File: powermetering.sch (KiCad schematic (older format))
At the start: 143 parts, among them J1 Conn_01x04, J2 Conn_01x02, J3 Conn_01x02, J4 Conn_01x02, J5 Conn_01x02, T1 Transformer_1P_1S, T2 Transformer_1P_1S, T3 Transformer_1P_1S, U2 ADE9000, U7 LTC4055, Y1 Crystal

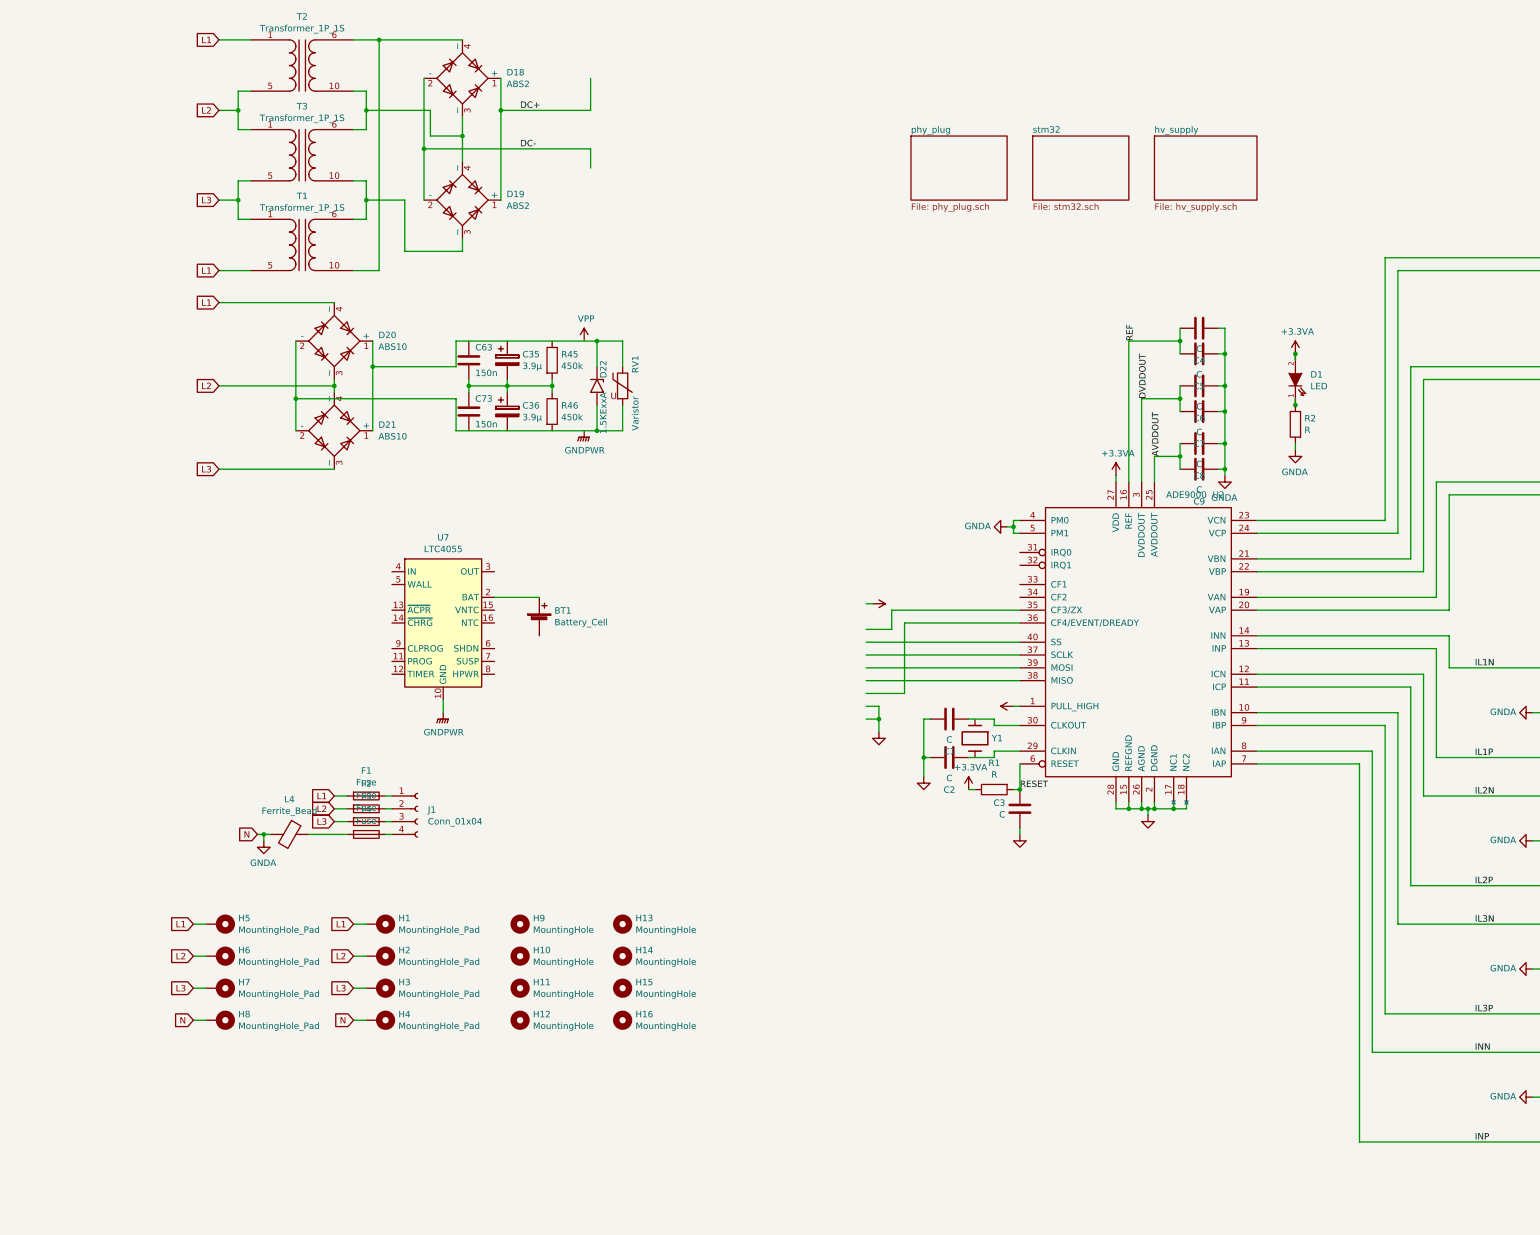
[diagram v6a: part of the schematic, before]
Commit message: add supply and AFE isolation
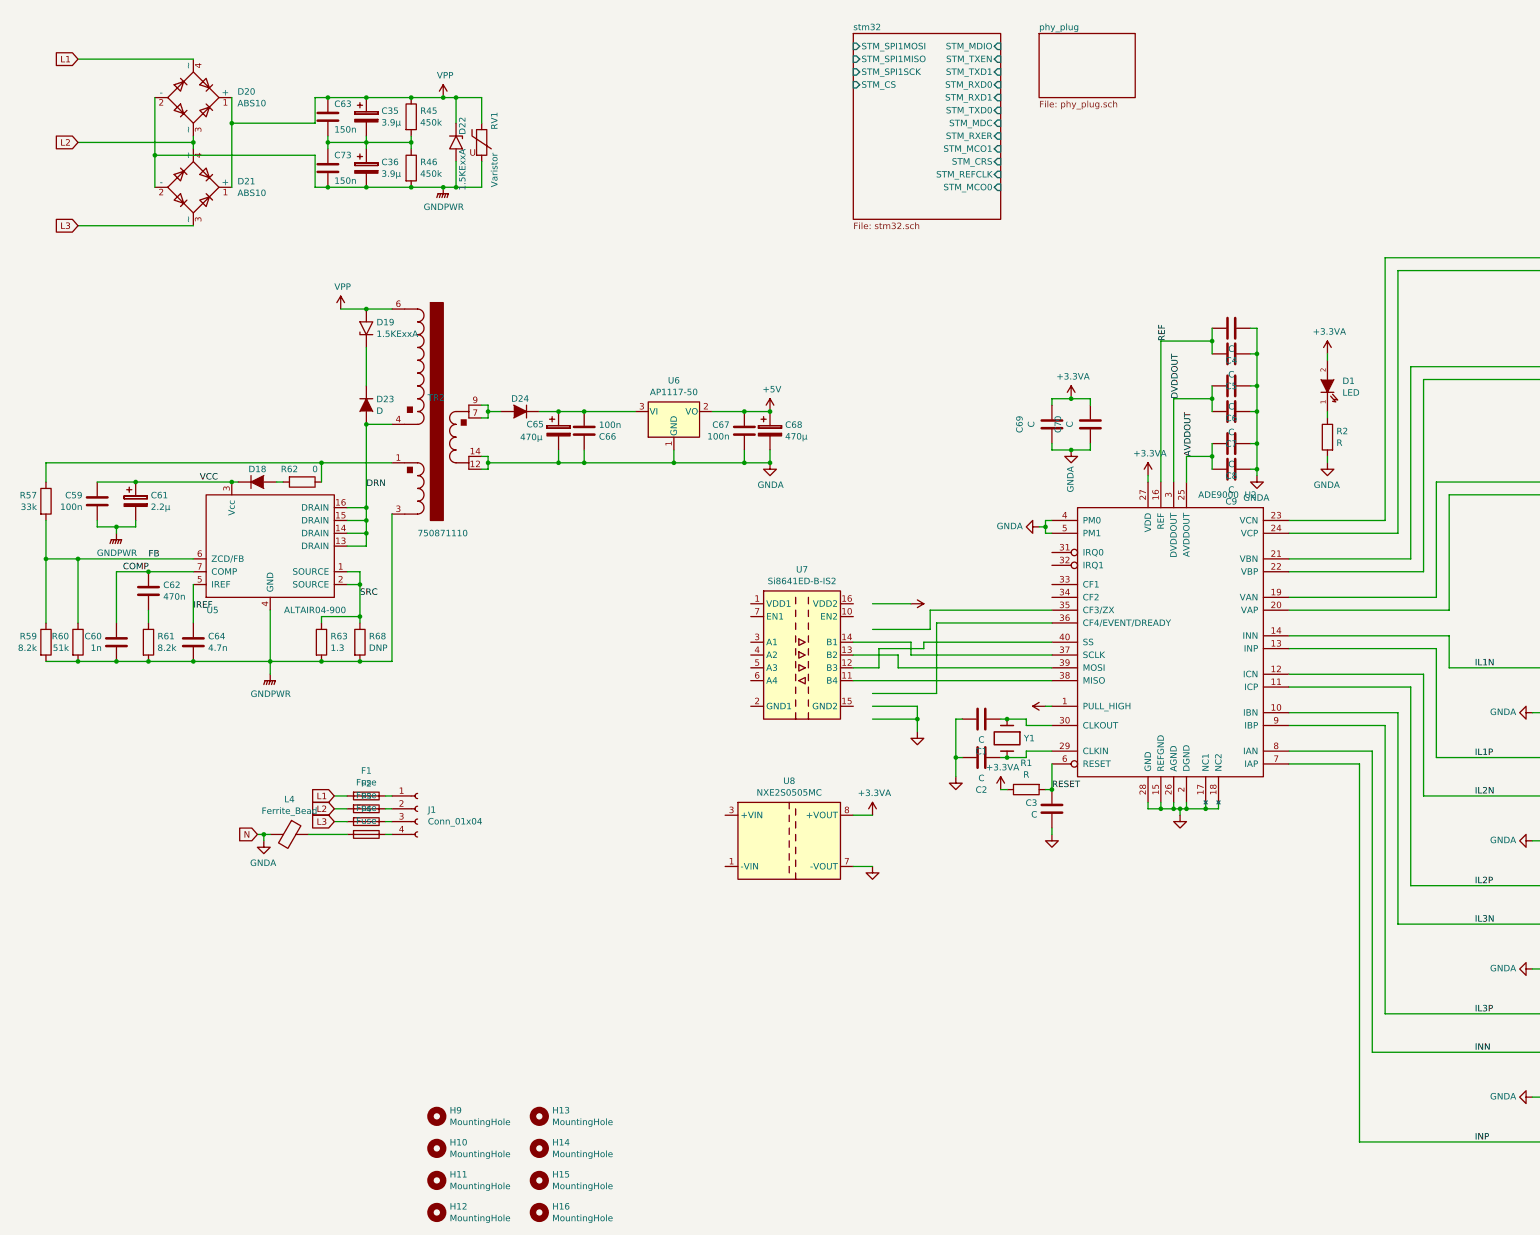
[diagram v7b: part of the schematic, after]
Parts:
- removed BT1: Battery_Cell, Battery:BatteryHolder_Keystone_1042_1x18650, symbol Device:Battery_Cell
- removed D18, D19: ABS2, Diode_SMD:Diode_Bridge_Diotec_ABS, symbol Diode_Bridge:ABS2
- removed H1, H2, H3, H4, H5, H6, H7, H8: MountingHole_Pad, MountingHole:MountingHole_3.2mm_M3_DIN965_Pad, symbol Mechanical:MountingHole_Pad
- removed T1, T2, T3: Transformer_1P_1S, Transformer_THT:Transformer_CHK_EI30-2VA_1xSec, symbol powermetering:Transformer_1P_1S
- removed U7: LTC4055, Package_DFN_QFN:QFN-16-1EP_4x4mm_P0.65mm_EP2.15x2.15mm, symbol Battery_Management:LTC4055
- added C59, C66, C67: 100n, stmbl:C_0805, symbol stmbl:C
- added C60: 1n, stmbl:C_0805, symbol stmbl:C
- added C61: 2.2µ, stmbl:C_1206, symbol stmbl:CP
- added C62: 470n, stmbl:C_0805, symbol stmbl:C
- added C64: 4.7n, stmbl:C_0805, symbol stmbl:C
- added C65: 470µ, Capacitor_SMD:CP_Elec_8x10, symbol stmbl:CP
- added C68: 470µ, Capacitor_SMD:CP_Elec_8x10.5, symbol stmbl:CP
- added C69, C70: C, stmbl:C_0603, symbol stmbl:C
- added D18, D23, D24: D, stmbl:SMA_Standard, symbol stmbl:D
- added D19: 1.5KExxA, stmbl:SMA_Standard, symbol Diode:1.5KExxA
- added R57: 33k, stmbl:R_0805, symbol stmbl:R
- added R59, R61: 8.2k, stmbl:R_0805, symbol stmbl:R
- added R60: 51k, stmbl:R_0805, symbol stmbl:R
- added R62: 0, stmbl:R_0805, symbol stmbl:R
- added R63: 1.3, stmbl:R_1206, symbol stmbl:R
- added R68: DNP, stmbl:R_1206, symbol stmbl:R
- added TR2: 750871110, altair04:750871110, symbol altair04:TRANSFO
- added U5: ALTAIR04-900, Package_SO:SOIC-16_3.9x9.9mm_P1.27mm, symbol altair04:ALTAIR04-900
- added U6: AP1117-50, Package_TO_SOT_SMD:SOT-223-3_TabPin2, symbol Regulator_Linear:AP1117-50
- added U7: Si8641ED-B-IS2, Package_SO:SOIC-16W_7.5x10.3mm_P1.27mm, symbol Isolator:Si8641ED-B-IS2
- added U8: NXE2S0505MC, Converter_DCDC:Converter_DCDC_muRata_NXE2SxxxxMC_THT, symbol Regulator_Switching:NXE2S0505MC
- C1, C10, C11, C12, C13, C14, C15, C16, C17, C18, C19, C2, C20, C21, C22, C23, C24, C25, C26, C27, C28, C29, C3, C30, C31, C32, C33, C34, C4, C5, C6, C7, C8, C9: footprint stmbl-kicad-lib:C_0603 -> stmbl:C_0603
- D10, D11, D12, D13, D14, D15, D16, D17, D2, D3, D4, D5, D6, D7, D8, D9: footprint stmbl-kicad-lib:SMA_Standard -> stmbl:SMA_Standard
- D22: footprint Diode_THT:D_DO-201AE_P15.24mm_Horizontal -> stmbl:SMA_Standard
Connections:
- net labels added: +5V, COMP, DRN, FB, IREF, SRC, VCC
- net labels removed: DC+, DC-
- wire segments 418 -> 472
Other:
- moved on the sheet: C1, C2, C3, C35, C36, C4, C5, C6, C63, C7, C73, C8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

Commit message: eth phy
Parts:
- added C71: C, stmbl:C_0603, symbol stmbl:C
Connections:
- net +3.3VA: now also U7.10 (EN2), U7.16 (VDD2), C71.2
- net GNDA: now also U7.15 (GND2), U7.9 (GND2), C71.1; no longer C65.2, C66.1, C67.2, C68.2, TR2.12, TR2.14, U6.1 (GND)
- net +3V3: now reaches U7.1 (VDD1)
- net +3V3: now also U7.7 (EN1)
- net GND: now reaches U7.2 (GND1), U7.8 (GND1)
- net GND: now also C65.2, C66.1, C67.2, C68.2, TR2.12, TR2.14, U6.1 (GND)
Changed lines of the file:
@@
 	8650 5400 7700 5400
 Wire Wire Line
-	7700 5400 7700 5550
-Wire Wire Line
-	7700 5550 7250 5550
-Wire Wire Line
 	8650 5500 7750 5500
-Wire Wire Line
-	7750 5500 7750 6050
-Wire Wire Line
-	7750 6050 7250 6050
 $Comp
 L power:GNDA #PWR0111
 U 1 1 5C65B751
-P 7600 6350
-F 0 "#PWR0111" H 7600 6100 50  0001 C CNN
-F 1 "GNDA" H 7605 6177 50  0001 C CNN
-F 2 "" H 7600 6350 50  0001 C CNN
-F 3 "" H 7600 6350 50  0001 C CNN
-	1    7600 6350
+P 7200 6250
+F 0 "#PWR0111" H 7200 6000 50  0001 C CNN
+F 1 "GNDA" H 7205 6077 50  0001 C CNN
+F 2 "" H 7200 6250 50  0001 C CNN
+F 3 "" H 7200 6250 50  0001 C CNN
+	1    7200 6250
 	-1   0    0    -1
 $EndComp
-Wire Wire Line
-	7250 6150 7600 6150
-Wire Wire Line
-	7600 6150 7600 6250
-Wire Wire Line
-	7250 6250 7600 6250
-Connection ~ 7600 6250
-Wire Wire Line
-	7600 6250 7600 6350
 $Comp
 L stmbl:Crystal Y1
@@
 $EndComp
 $Comp
-L power:+3.3VA #PWR0119
+L stmbl:+3.3VA #PWR0119
 U 1 1 5CC2E852
-P 7550 5350
-F 0 "#PWR0119" H 7550 5200 50  0001 C CNN
-F 1 "+3.3VA" V 7565 5478 50  0001 L CNN
-F 2 "" H 7550 5350 50  0001 C CNN
-F 3 "" H 7550 5350 50  0001 C CNN
-	1    7550 5350
-	0    1    1    0
-$EndComp
-Wire Wire Line
-	7250 5350 7550 5350
+P 7200 5250
+F 0 "#PWR0119" H 7200 5100 50  0001 C CNN
+F 1 "+3.3VA" V 7215 5378 50  0001 L CNN
+F 2 "" H 7200 5250 50  0001 C CNN
+F 3 "" H 7200 5250 50  0001 C CNN
+	1    7200 5250
+	1    0    0    -1
+$EndComp
 $Comp
 L power:+3.3VA #PWR0120
@@
 	1650 1850 1650 2100
 $Sheet
-S 8550 900  750  500
+S 8550 900  1250 1450
 U 5D9E2522
 F0 "phy_plug" 50
 F1 "phy_plug.sch" 50
+F2 "LED1K" I L 8550 2250 50
+F3 "PHY_RST" I L 8550 2150 50
+F4 "PHY_CRS" I L 8550 1900 50
+F5 "PHY_TXD1" I L 8550 1300 50
+F6 "PHY_TXD0" I L 8550 1200 50
+F7 "PHY_TXEN" I L 8550 1100 50
+F8 "PHY_RXD0" I L 8550 1400 50
+F9 "PHY_RXD1" I L 8550 1500 50
+F10 "PHY_MDC" I L 8550 1600 50
+F11 "PHY_MDIO" I L 8550 1000 50
+F12 "PHY_XI" I L 8550 1800 50
+F13 "PHY_X0" I R 9800 2200 50
+F14 "PHY_INTRP" I R 9800 2100 50
+F15 "PHY_REFCLK" I L 8550 2000 50
 $EndSheet
 $Sheet
@@
 F2 "STM_MDIO" I R 8250 1000 50
 F3 "STM_TXEN" I R 8250 1100 50
-F4 "STM_TXD1" I R 8250 1200 50
-F5 "STM_RXD0" I R 8250 1300 50
-F6 "STM_RXD1" I R 8250 1400 50
-F7 "STM_TXD0" I R 8250 1500 50
+F4 "STM_TXD1" I R 8250 1300 50
+F5 "STM_RXD0" I R 8250 1400 50
+F6 "STM_RXD1" I R 8250 1500 50
+F7 "STM_TXD0" I R 8250 1200 50
 F8 "STM_MDC" I R 8250 1600 50
-F9 "STM_RXER" I R 8250 1700 50
-F10 "STM_MCO1" I R 8250 1800 50
-F11 "STM_CRS" I R 8250 1900 50
-F12 "STM_SPI1MOSI" I L 7100 1000 50
-F13 "STM_SPI1MISO" I L 7100 1100 50
-F14 "STM_SPI1SCK" I L 7100 1200 50
-F15 "STM_CS" I L 7100 1300 50
-F16 "STM_REFCLK" I R 8250 2000 50
-F17 "STM_MCO0" I R 8250 2100 50
+F9 "STM_MCO1" I R 8250 1800 50
+F10 "STM_CRS" I R 8250 1900 50
+F11 "STM_SPI1MOSI" I L 7100 1000 50
+F12 "STM_SPI1MISO" I L 7100 1100 50
+F13 "STM_SPI1SCK" I L 7100 1200 50
+F14 "STM_CS" I L 7100 1300 50
+F15 "STM_REFCLK" I R 8250 2000 50
+F16 "STM_MCO0" I R 8250 2100 50
 $EndSheet
 $Comp
@@
 $EndComp
 $Comp
-L stmbl:GNDA #PWR0158
+L stmbl:GND #PWR0158
 U 1 1 5CF1BEF6
 P 6450 4250
 F 0 "#PWR0158" H 6450 4000 50  0001 C CNN
-F 1 "GNDA" H 6455 4077 50  0000 C CNN
+F 1 "GND" H 6455 4077 50  0000 C CNN
 F 2 "" H 6450 4250 50  0001 C CNN
 F 3 "" H 6450 4250 50  0001 C CNN
@@
 	7550 5650 7100 5650
 Wire Wire Line
-	8650 5850 7450 5850
-Wire Wire Line
-	7450 5850 7450 5750
-Wire Wire Line
-	7450 5750 7100 5750
+	8650 5850 7500 5850
+Wire Wire Line
+	7500 5850 7500 5750
+Wire Wire Line
+	7500 5750 7100 5750
 Wire Wire Line
 	8650 5650 7650 5650
@@
 	7650 5650 7650 5700
 Wire Wire Line
-	7650 5700 7300 5700
-Wire Wire Line
-	7300 5700 7300 5850
-Wire Wire Line
-	7300 5850 7100 5850
+	7650 5700 7400 5700
+Wire Wire Line
+	7400 5700 7400 5850
+Wire Wire Line
+	7400 5850 7100 5850
 $Comp
 L Regulator_Switching:NXE2S0505MC U8
@@
 Wire Wire Line
 	8800 4150 8950 4150
+Wire Wire Line
+	7100 6150 7200 6150
+Wire Wire Line
+	7200 6150 7200 6250
+Wire Wire Line
+	7200 5250 7200 5350
+Wire Wire Line
+	7100 5350 7200 5350
+Wire Wire Line
+	7200 5350 7200 5450
+Wire Wire Line
+	7100 5450 7200 5450
+Connection ~ 7200 5350
+$Comp
+L stmbl:GND #PWR0166
+U 1 1 5DB7D3E6
+P 6150 6250
+F 0 "#PWR0166" H 6150 6000 50  0001 C CNN
+F 1 "GND" H 6155 6077 50  0000 C CNN
+F 2 "" H 6150 6250 50  0001 C CNN
+F 3 "" H 6150 6250 50  0001 C CNN
+	1    6150 6250
+	1    0    0    -1
+$EndComp
+Wire Wire Line
+	6300 6150 6150 6150
+Wire Wire Line
+	6150 6150 6150 6250
+$Comp
+L stmbl:+3.3V #PWR0167
+U 1 1 5DBC667B
+P 6200 5250
+F 0 "#PWR0167" H 6200 5100 50  0001 C CNN
+F 1 "+3.3V" V 6215 5378 50  0001 L CNN
+F 2 "" H 6200 5250 50  0001 C CNN
+F 3 "" H 6200 5250 50  0001 C CNN
+	1    6200 5250
+	1    0    0    -1
+$EndComp
+Wire Wire Line
+	6200 5250 6200 5350
+Wire Wire Line
+	6200 5450 6300 5450
+Wire Wire Line
+	6300 5350 6200 5350
+Connection ~ 6200 5350
+Wire Wire Line
+	6200 5350 6200 5450
+$Comp
+L stmbl:C C71
+U 1 1 5DC59411
+P 8400 3950
+F 0 "C71" V 8148 3950 50  0000 C CNN
+F 1 "C" V 8239 3950 50  0000 C CNN
+F 2 "stmbl:C_0603" H 8438 3800 50  0001 C CNN
+F 3 "" H 8400 3950 50  0001 C CNN
+	1    8400 3950
+	1    0    0    1
+$EndComp
+Wire Wire Line
+	8650 3750 8400 3750
+Wire Wire Line
+	8400 3750 8400 3800
+Connection ~ 8650 3750
+Wire Wire Line
+	8400 4100 8400 4150
+Wire Wire Line
+	8400 4150 8650 4150
+Connection ~ 8650 4150
+Wire Wire Line
+	8250 1000 8550 1000
+Wire Wire Line
+	8250 1100 8550 1100
+Wire Wire Line
+	8250 1200 8550 1200
+Wire Wire Line
+	8250 1300 8550 1300
+Wire Wire Line
+	8250 1400 8550 1400
+Wire Wire Line
+	8250 1500 8550 1500
+Wire Wire Line
+	8250 1600 8550 1600
+Wire Wire Line
+	8250 1800 8550 1800
+Wire Wire Line
+	8250 1900 8550 1900
+Wire Wire Line
+	8250 2000 8550 2000
 $EndSCHEMATC
